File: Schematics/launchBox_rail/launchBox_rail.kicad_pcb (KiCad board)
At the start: 2 copper layers, 15 parts, among them J1 Screw_Terminal_01x02, J2 Screw_Terminal_01x02, J3 RadioConnectorRxTx, J4 RadioConnectorPWR, Q1 NMOS, SW1 SW_MEC_5G

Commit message: v1 of PCB for LPB is complete
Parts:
- removed J3: RadioConnectorRxTx, Connector_PinHeader_1.00mm:PinHeader_1x02_P1.00mm_Vertical
- removed J4: RadioConnectorPWR, Connector_PinHeader_1.00mm:PinHeader_1x02_P1.00mm_Vertical
- added J5: Conn_01x04_Pin, Connector_PinHeader_2.54mm:PinHeader_1x04_P2.54mm_Vertical, F.Cu at (110.0, 67.4)
- BZ1, J2: footprint Connector_PinHeader_1.00mm:PinHeader_1x02_P1.00mm_Vertical -> Connector_PinHeader_2.54mm:PinHeader_1x02_P2.54mm_Vertical
- J1, SW1: footprint Connector_PinHeader_1.00mm:PinHeader_1x03_P1.00mm_Vertical -> Connector_PinHeader_2.54mm:PinHeader_1x02_P2.54mm_Vertical
- Q1: footprint Connector_PinHeader_1.00mm:PinHeader_1x03_P1.00mm_Vertical -> Connector_PinHeader_2.54mm:PinHeader_1x03_P2.54mm_Vertical
- moved R3 33.6 mm to (148.0, 89.2), turned to 90 degrees
- moved R4 18.6 mm to (146.0, 76.2), turned to 90 degrees
- moved J1 11.2 mm to (143.5, 91.5)
- moved R6 10.0 mm to (138.9, 90.5)
- moved R7 10.0 mm to (135.5, 89.7)
- moved BZ1 1.50 mm to (106.0, 91.0)
- moved Q1 0.28 mm to (135.2, 56.5)
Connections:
- A2 pad 1: Net-(A2-D1/TX) -> /radioTx
- A2 pad 2: Net-(A2-D0/RX) -> /radioRx
- A2 pad 26: unconnected-(A2-A7-Pad26) -> /continuity
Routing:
- net Net-(J1-Pin_2): track 0.00 -> 49.0 mm
- net /trigger: track 0.00 -> 48.8 mm
- net /radioPWR: track 0.00 -> 27.0 mm
- net /continuity: track 0.00 -> 26.4 mm
- net +12V: track 0.00 -> 15.9 mm
- net Net-(Q1-G): track 0.00 -> 8.92 mm
- net /radioTx: track 0.00 -> 7.25 mm
- net /radioRx: track 0.00 -> 6.46 mm
- net Net-(A2-D6): track 0.00 -> 4.86 mm
- net Net-(J1-Pin_1): track 0.00 -> 4.20 mm
- net Net-(A2-A4): track 0.00 -> 4.09 mm
- net Net-(BZ1-+): track 0.00 -> 3.87 mm
- net GNDREF: track 0.00 -> 1.36 mm
- added copper zone on B.Cu, net GNDREF

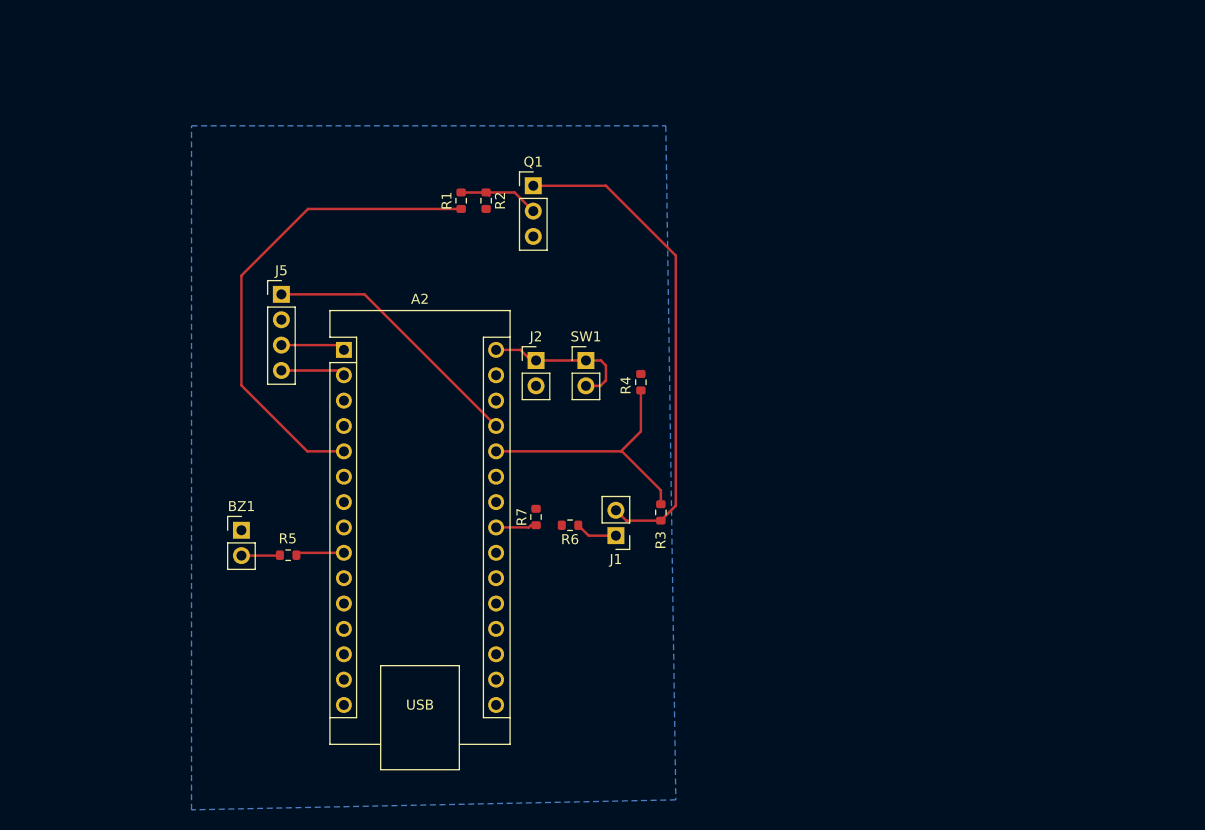
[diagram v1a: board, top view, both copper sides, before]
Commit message: Finished LPB PCB design
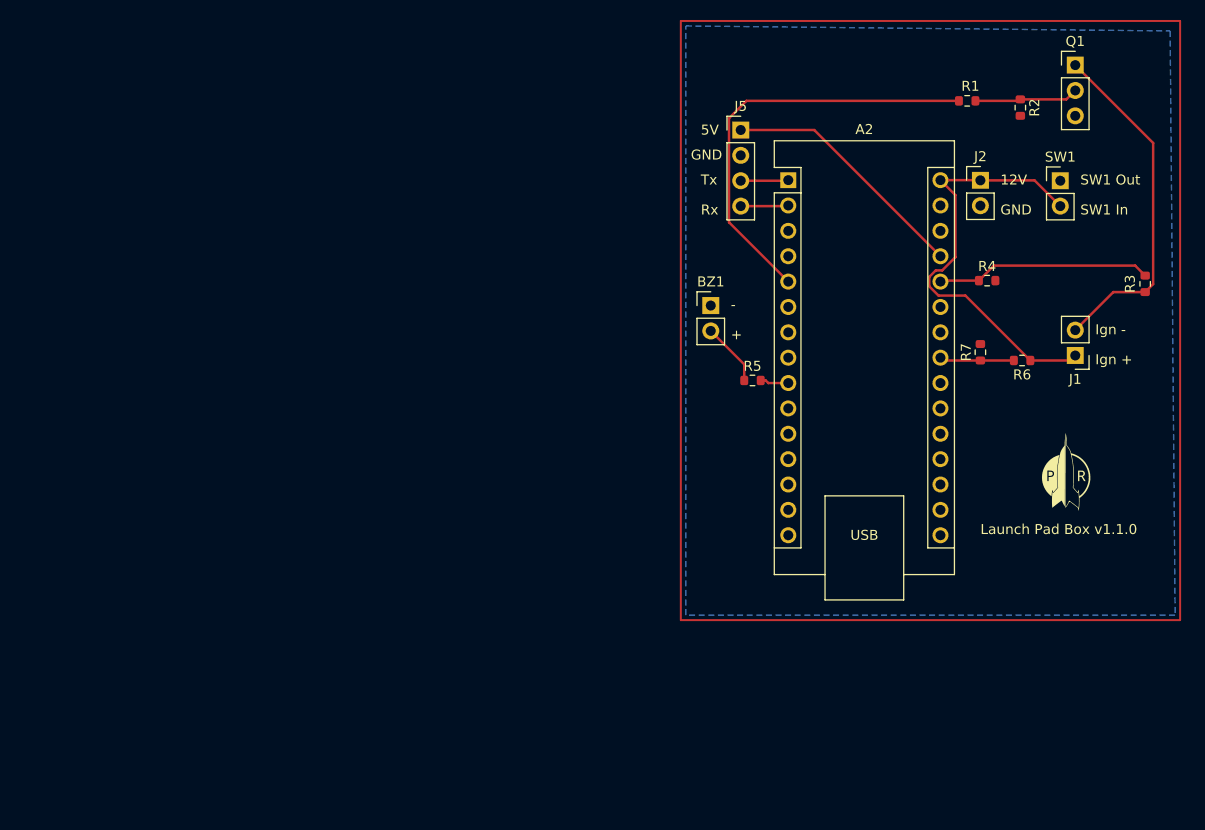
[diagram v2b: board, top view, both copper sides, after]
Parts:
- added G***: LOGO, logo:Logo, F.Cu at (188.5, 85.0)
- moved Q1 55.6 mm to (189.5, 44.4)
- moved R2 54.3 mm to (184.0, 48.7)
- moved R3 53.6 mm to (196.5, 66.3)
- moved BZ1 52.1 mm to (153.0, 68.5)
- moved R1 51.7 mm to (178.7, 48.0), turned to 0 degrees
- moved SW1 50.8 mm to (188.0, 56.0)
- moved R5 49.7 mm to (157.2, 76.0)
- moved J1 49.4 mm to (189.5, 73.5)
- moved J5 48.9 mm to (156.0, 50.9)
- moved R6 48.2 mm to (184.2, 74.0)
- moved J2 48.0 mm to (180.0, 56.0)
- moved A2 47.6 mm to (160.8, 55.9)
- moved R7 47.5 mm to (180.0, 73.2)
- moved R4 36.1 mm to (180.7, 66.0), turned to 0 degrees
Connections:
- J1 pad 1: Net-(J1-Pin_1) -> +12V
- R6 pad 1: Net-(J1-Pin_1) -> +12V
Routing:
- net +12V: track 15.9 -> 43.8 mm
- net Net-(J1-Pin_2): track 49.0 -> 34.9 mm
- net /trigger: track 48.8 -> 42.6 mm
- net /continuity: track 26.4 -> 21.6 mm
- net Net-(J1-Pin_1): track 4.20 -> 0.00 mm
- net Net-(A2-A4): track 4.09 -> 7.47 mm
- net Net-(BZ1-+): track 3.87 -> 6.35 mm
- net /radioTx: track 7.25 -> 4.78 mm
- net Net-(A2-D6): track 4.86 -> 2.87 mm
- net /radioPWR: track 27.0 -> 25.2 mm
- net /radioRx: track 6.46 -> 4.78 mm
- net Net-(Q1-G): track 8.92 -> 10.4 mm
- net GNDREF: track 1.36 -> 0.03 mm
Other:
- board text added: "+"
- board text added: "-"
- board text added: "12V"
- board text added: "5V"
- board text added: "GND"
- board text added: "Ign +"
- board text added: "Ign -"
- board text added: "Launch Pad Box v1.1.0"
- board text added: "Rx"
- board text added: "SW1 In"
- board text added: "SW1 Out"
- board text added: "Tx"

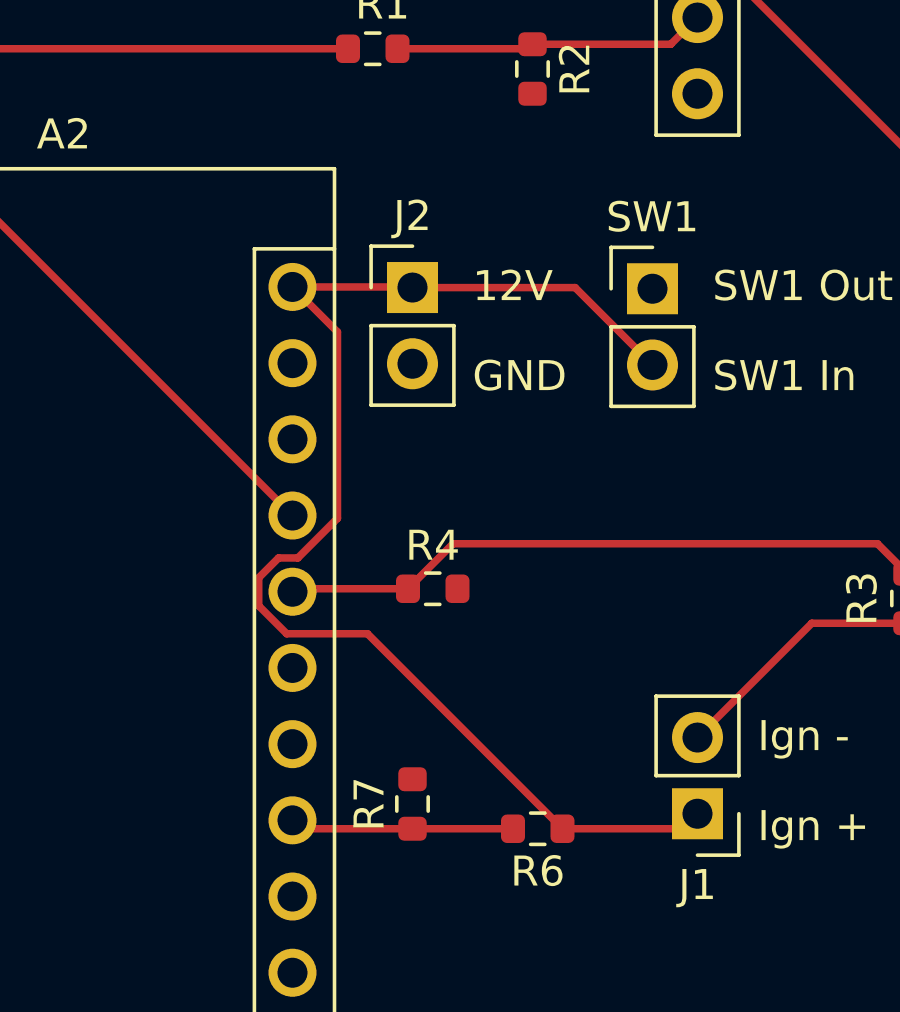
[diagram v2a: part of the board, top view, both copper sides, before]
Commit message: Fixed short
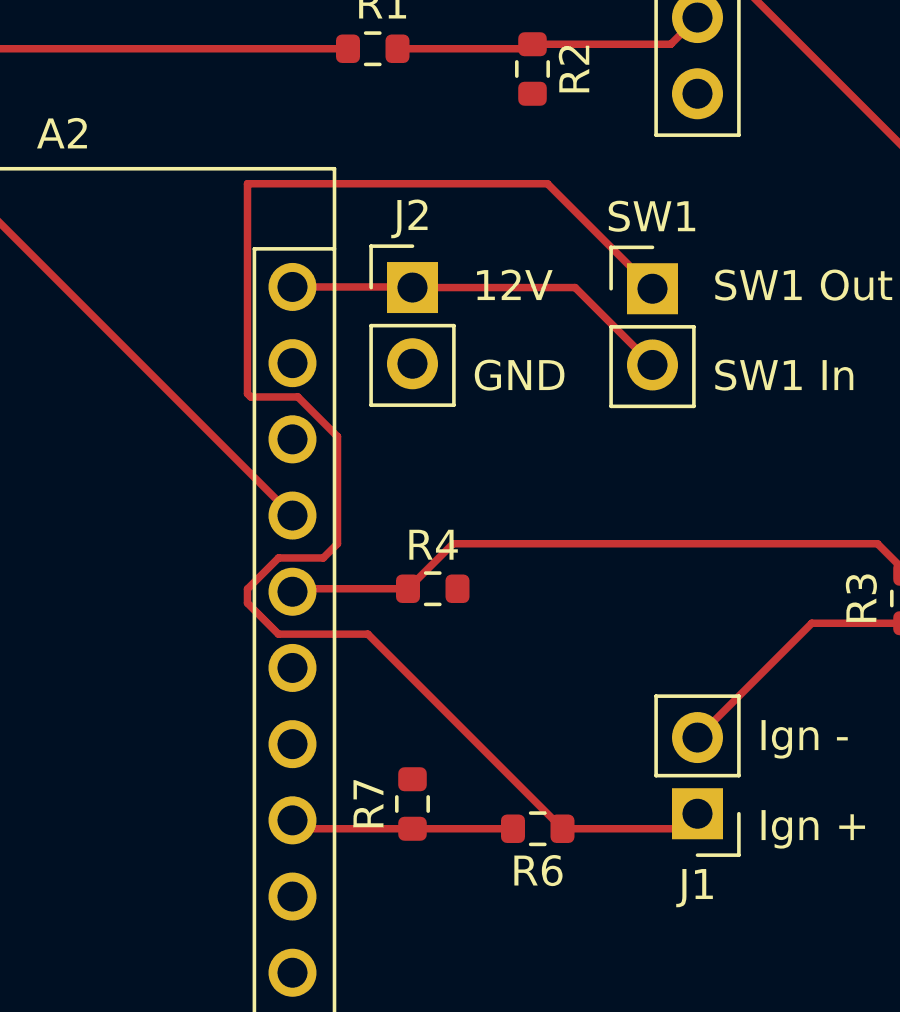
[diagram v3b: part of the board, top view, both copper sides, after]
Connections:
- J1 pad 1: +12V -> Net-(J1-Pin_1)
- R6 pad 1: +12V -> Net-(J1-Pin_1)
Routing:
- net +12V: track 43.8 -> 64.6 mm

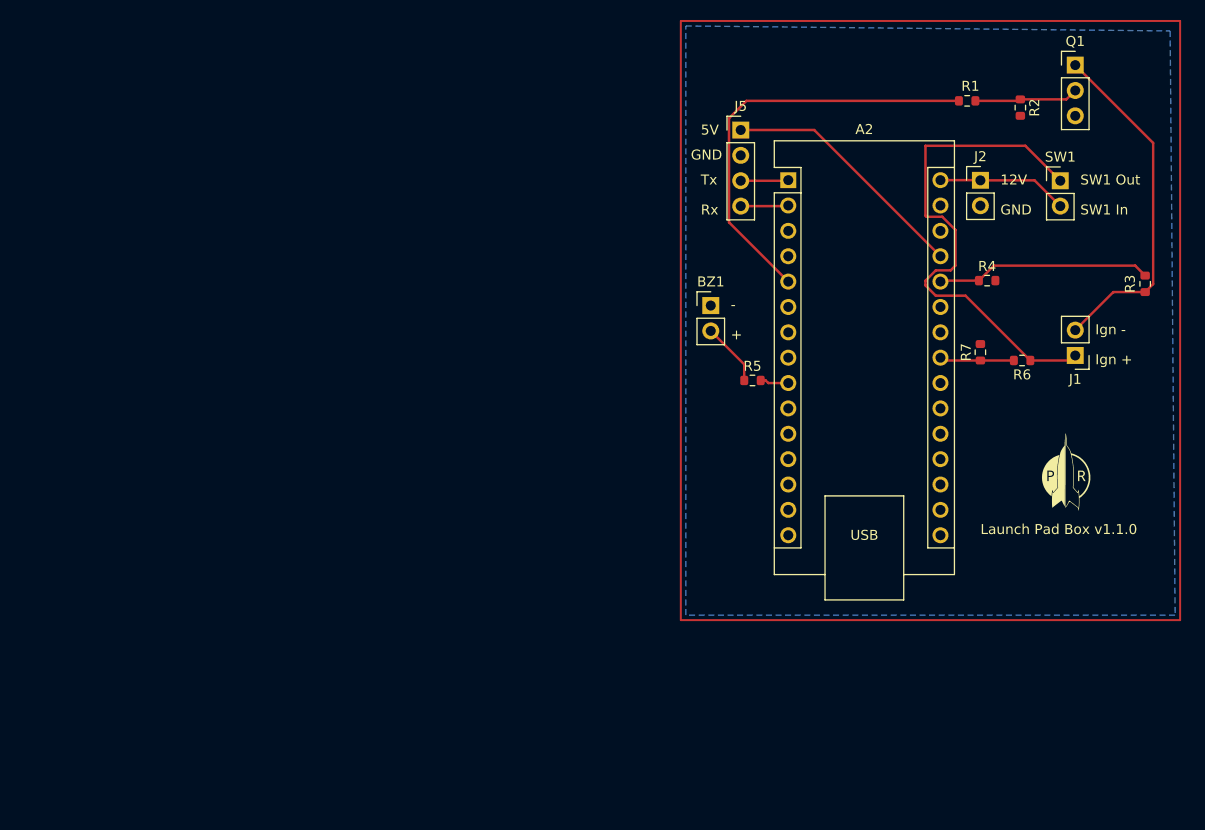
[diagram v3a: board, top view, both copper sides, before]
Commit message: Cleaned up rail side launch box schematic and PCB
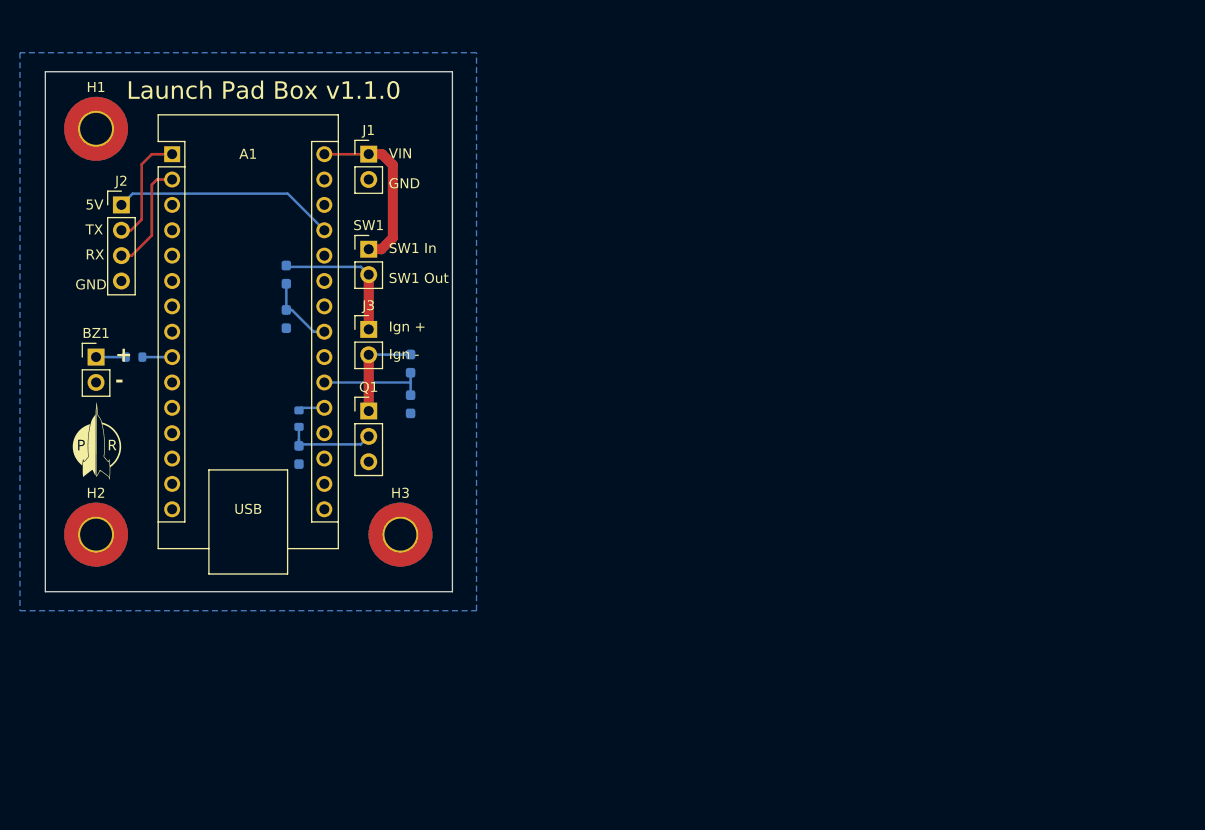
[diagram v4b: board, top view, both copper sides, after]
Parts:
- added H1: MountingHole_Pad, MountingHole:MountingHole_3.2mm_M3_Pad_TopBottom, F.Cu at (91.4, 50.8)
- added H2: MountingHole_Pad, MountingHole:MountingHole_3.2mm_M3_Pad_TopBottom, F.Cu at (91.4, 91.4)
- added H3: MountingHole_Pad, MountingHole:MountingHole_3.2mm_M3_Pad_TopBottom, F.Cu at (121.9, 91.4)
- R1: value 500 -> 7.5k; footprint Resistor_SMD:R_0603_1608Metric -> Resistor_SMD:R_0603_1608Metric_Pad0.98x0.95mm_HandSolder; moved to B.Cu
- R2: value 10k -> 7.5k; footprint Resistor_SMD:R_0603_1608Metric -> Resistor_SMD:R_0603_1608Metric_Pad0.98x0.95mm_HandSolder; moved to B.Cu
- R3: value 7.5k -> 500; moved to B.Cu
- R4: value 3k -> 10k; moved to B.Cu
- R5: value 10k -> 3k; footprint Resistor_SMD:R_0603_1608Metric -> Resistor_SMD:R_0603_1608Metric_Pad0.98x0.95mm_HandSolder; moved to B.Cu
- R6: value 7.5k -> 10k; footprint Resistor_SMD:R_0603_1608Metric -> Resistor_SMD:R_0603_1608Metric_Pad0.98x0.95mm_HandSolder; moved to B.Cu
- R7: footprint Resistor_SMD:R_0603_1608Metric -> Resistor_SMD:R_0603_1608Metric_Pad0.98x0.95mm_HandSolder; moved to B.Cu
- moved G*** 97.1 mm to (91.4, 81.9)
- moved R3 85.8 mm to (111.8, 79.8), turned to -90 degrees
- moved R4 85.8 mm to (95.2, 73.7)
- moved Q1 78.8 mm to (118.7, 79.1)
- moved R6 73.0 mm to (111.8, 83.5), turned to -90 degrees
- moved J3 70.8 mm to (118.7, 70.9), turned to 0 degrees
- moved R1 70.4 mm to (110.5, 65.4), turned to -90 degrees
- moved SW1 69.6 mm to (118.7, 62.9)
- moved R2 66.2 mm to (122.9, 74.3)
- moved J2 62.5 mm to (94.0, 58.4)
- moved BZ1 61.8 mm to (91.4, 73.7)
- moved A1 61.8 mm to (99.1, 53.3)
- moved J1 61.3 mm to (118.7, 53.3)
- moved R7 57.3 mm to (122.9, 78.4), turned to -90 degrees
- moved R5 47.1 mm to (110.5, 69.8), turned to -90 degrees
- renumbered A2 to A1, J2 to J1, J5 to J2, J1 to J3
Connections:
- net /radioPWR renamed +5V
- A1 pad 20: unconnected-(A2-A1-Pad20) -> /trigger
- A1 pad 21: unconnected-(A2-A2-Pad21) -> /continuity
- A1 pad 23: Net-(A2-A4) -> /armed
- A1 pad 26: /continuity -> unconnected-(A1-A7-Pad26)
- A1 pad 29: GNDREF -> GND
- A1 pad 30: +12V -> VIN
- A1 pad 4: GNDREF -> GND
- A1 pad 5: /trigger -> unconnected-(A1-D2-Pad5)
- A1 pad 9: Net-(A2-D6) -> Net-(A1-D6)
- BZ1 pad 1: GNDREF -> Net-(BZ1--)
- BZ1 pad 2: Net-(BZ1-+) -> GND
- J1 pad 1: +12V -> VIN
- J1 pad 2: GNDREF -> GND
- J2 pad 2: GNDREF -> /radioTx
- J2 pad 3: /radioTx -> /radioRx
- J2 pad 4: /radioRx -> GND
- J3 pad 1: Net-(J1-Pin_1) -> /pyro_power
- J3 pad 2: Net-(J1-Pin_2) -> Net-(J3-Pin_2)
- Q1 pad 1: Net-(J1-Pin_2) -> Net-(J3-Pin_2)
- Q1 pad 3: GNDREF -> GND
- R1 pad 1: /trigger -> /pyro_power
- R1 pad 2: Net-(Q1-G) -> /armed
- R2 pad 1: Net-(Q1-G) -> Net-(J3-Pin_2)
- R2 pad 2: GNDREF -> /continuity
- R3 pad 1: Net-(J1-Pin_2) -> /trigger
- R3 pad 2: /continuity -> Net-(Q1-G)
- R4 pad 1: /continuity -> Net-(BZ1--)
- R4 pad 2: GNDREF -> Net-(A1-D6)
- R5 pad 1: Net-(BZ1-+) -> /armed
- R5 pad 2: Net-(A2-D6) -> GND
- R6 pad 1: Net-(J1-Pin_1) -> Net-(Q1-G)
- R6 pad 2: Net-(A2-A4) -> GND
- R7 pad 1: Net-(A2-A4) -> /continuity
- R7 pad 2: GNDREF -> GND
- SW1 pad 1: +12V -> VIN
- SW1 pad 2: +12V -> /pyro_power
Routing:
- net +12V: track 64.6 -> 0.00 mm
- net /trigger: track 42.6 -> 2.65 mm
- net Net-(J1-Pin_2): track 34.9 -> 0.00 mm
- net VIN: track 0.00 -> 17.5 mm
- net /pyro_power: track 0.00 -> 14.1 mm
- net /continuity: track 21.6 -> 10.9 mm
- net Net-(J3-Pin_2): track 0.00 -> 9.83 mm
- net Net-(A2-A4): track 7.47 -> 0.00 mm
- net /armed: track 0.00 -> 7.33 mm
- net /radioTx: track 4.78 -> 11.5 mm
- net /radioRx: track 4.78 -> 11.2 mm
- net Net-(BZ1-+): track 6.35 -> 0.00 mm
- net Net-(BZ1--): track 0.00 -> 2.98 mm
- net Net-(A1-D6): track 0.00 -> 2.98 mm
- net +5V: track 25.2 -> 22.3 mm
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- added copper zone on B.Cu, net GND
- removed copper zone on B.Cu, net GNDREF
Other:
- board outline added: 40.8 x 52.1 mm
- board text added: "RX"
- board text added: "TX"
- board text added: "VIN"
- board text removed: "12V"
- board text removed: "Rx"
- board text removed: "Tx"

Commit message: Clean it up a bit more
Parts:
- moved R5 2.03 mm to (110.5, 71.9)
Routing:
- net /armed: track 7.33 -> 8.52 mm
- net +5V: track 22.3 -> 21.4 mm
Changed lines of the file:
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@@
 	(footprint "Resistor_SMD:R_0603_1608Metric_Pad0.98x0.95mm_HandSolder"
 		(layer "B.Cu")
-		(at 110.49 69.85 -90)
+		(at 110.49 71.882 -90)
 		(descr "Resistor SMD 0603 (1608 Metric), square (rectangular) end terminal, IPC-7351 nominal with elongated pad for handsoldering. (Body size source: IPC-SM-782 page 72, https://www.pcb-3d.com/wordpress/wp-content/uploads/ipc-sm-782a_amendment_1_and_2.pdf), generated with kicad-footprint-generator")
 		(tags "resistor handsolder")
@@
 	)
 	(gr_text "SW1 Out"
-		(at 120.745 66.36 0)
+		(at 120.396 66.36 0)
 		(layer "F.SilkS")
 		(effects
@@
 	)
 	(gr_text "SW1 In"
-		(at 120.745 63.36 0)
+		(at 120.396 63.36 0)
 		(layer "F.SilkS")
 		(effects
@@
 	)
 	(segment
-		(start 110.634 57.294)
+		(start 93.98 58.42)
+		(end 96.012 58.42)
+		(width 0.25)
+		(layer "B.Cu")
+		(net 11)
+	)
+	(segment
+		(start 110.64 60.96)
 		(end 114.3 60.96)
 		(width 0.25)
@@
 	)
 	(segment
-		(start 95.106 57.294)
-		(end 110.634 57.294)
+		(start 97.302 59.71)
+		(end 109.39 59.71)
 		(width 0.25)
 		(layer "B.Cu")
@@
 	)
 	(segment
-		(start 93.98 58.42)
-		(end 95.106 57.294)
+		(start 109.39 59.71)
+		(end 110.64 60.96)
 		(width 0.25)
 		(layer "B.Cu")
@@
 	)
 	(segment
+		(start 96.012 58.42)
+		(end 97.302 59.71)
+		(width 0.25)
+		(layer "B.Cu")
+		(net 11)
+	)
+	(segment
+		(start 110.49 70.9695)
+		(end 110.6405 71.12)
+		(width 0.25)
+		(layer "B.Cu")
+		(net 13)
+	)
+	(segment
+		(start 110.6405 71.12)
+		(end 114.3 71.12)
+		(width 0.25)
+		(layer "B.Cu")
+		(net 13)
+	)
+	(segment
 		(start 110.49 66.3175)
-		(end 110.49 68.9375)
-		(width 0.25)
-		(layer "B.Cu")
-		(net 13)
-	)
-	(segment
-		(start 113.23225 71.12)
-		(end 114.3 71.12)
-		(width 0.25)
-		(layer "B.Cu")
-		(net 13)
-	)
-	(segment
-		(start 111.04975 68.9375)
-		(end 113.23225 71.12)
-		(width 0.25)
-		(layer "B.Cu")
-		(net 13)
-	)
-	(segment
-		(start 110.49 68.9375)
-		(end 111.04975 68.9375)
-		(width 0.25)
-		(layer "B.Cu")
+		(end 110.49 70.9695)
+		(width 0.25)
+		(layer "B.Cu")
